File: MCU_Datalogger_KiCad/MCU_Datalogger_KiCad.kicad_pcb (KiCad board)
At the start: 2 copper layers, 29 parts, among them J1 Conn_01x04_Male, J2 Conn_01x04_Male, J3 Conn_01x09_Male, J4 Conn_02x03_Odd_Even, U1 24LC1025, U2 DS1337S+, U3 24LC1025, U4 ATMEGA328P-AU, Y1 32.768 KHz, Y2 16 MHz

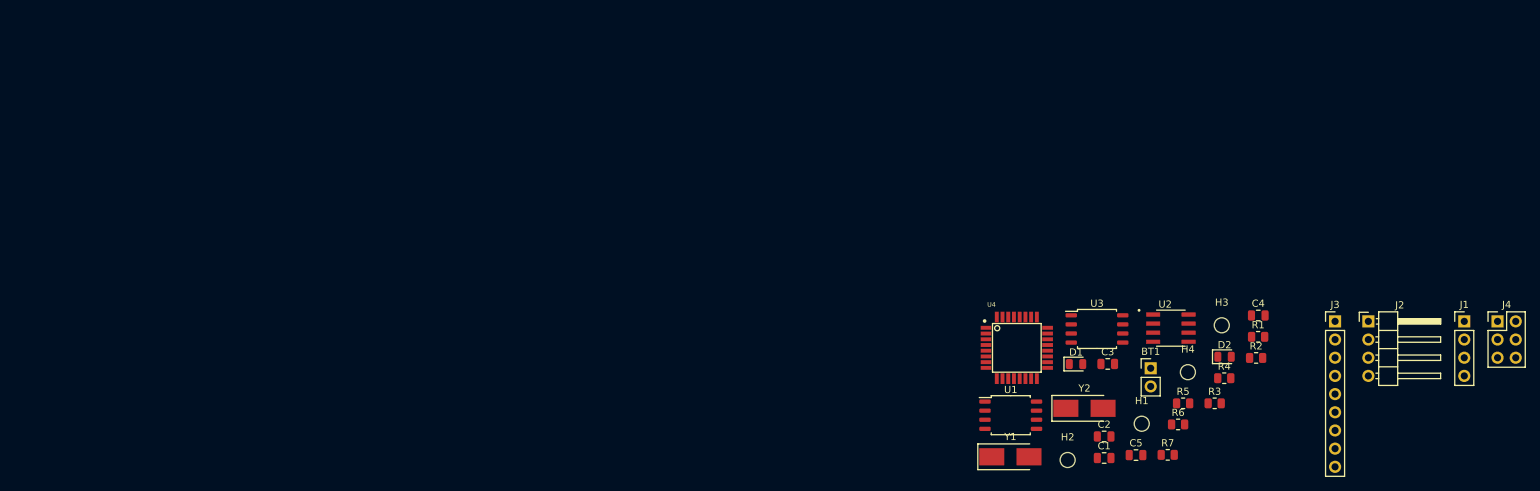
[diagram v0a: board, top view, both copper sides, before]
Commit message: Placement of footprints
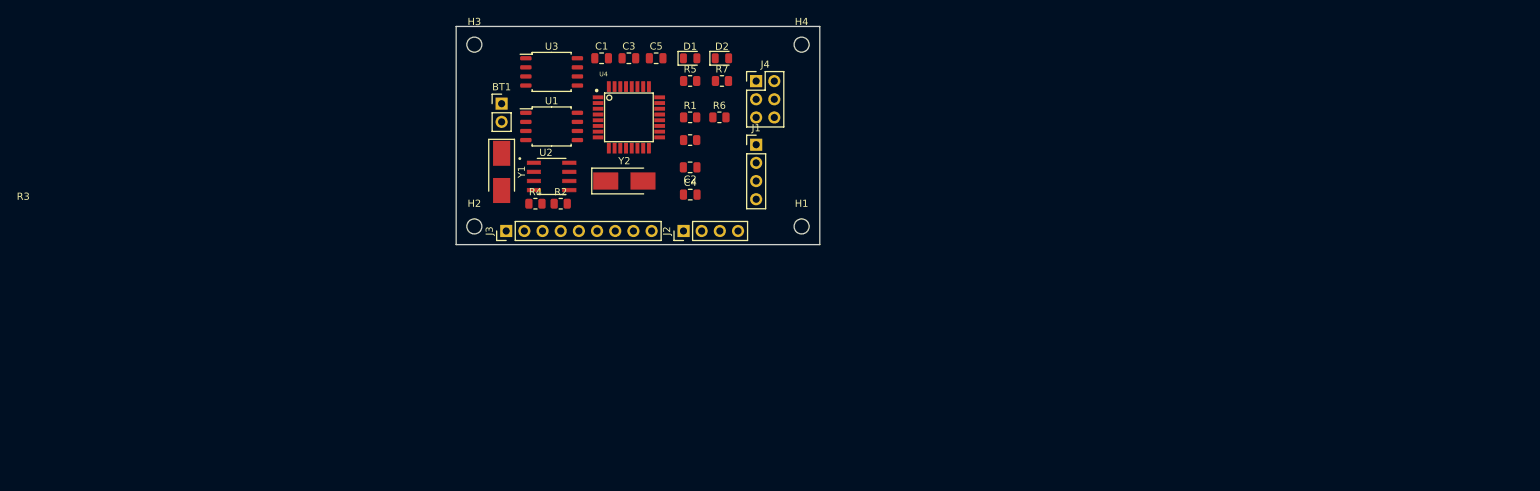
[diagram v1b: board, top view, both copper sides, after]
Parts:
- J2: footprint Connector_PinHeader_2.54mm:PinHeader_1x04_P2.54mm_Horizontal -> Connector_PinHeader_2.54mm:PinHeader_1x04_P2.54mm_Vertical
- moved J3 116.5 mm to (32.4, 66.7), turned to 90 degrees
- moved H3 111.5 mm to (27.9, 40.6)
- moved J4 108.9 mm to (67.3, 45.7)
- moved J1 102.0 mm to (67.3, 54.6)
- moved R2 99.5 mm to (40.0, 62.9)
- moved R4 99.3 mm to (36.5, 62.9)
- moved BT1 97.9 mm to (31.8, 48.9)
- moved J2 96.5 mm to (57.2, 66.7), turned to 90 degrees
- moved C1 89.7 mm to (45.7, 42.5)
- moved H2 89.1 mm to (27.9, 66.0)
- moved U2 89.1 mm to (38.7, 59.1)
- moved C5 87.0 mm to (53.3, 42.5)
- moved R1 85.1 mm to (58.1, 50.8)
- moved U3 84.2 mm to (38.7, 44.5)
- moved R5 82.3 mm to (58.1, 45.7)
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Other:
- board outline added: 50.8 x 30.5 mm

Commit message: Routing
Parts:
- moved D1 4.41 mm to (62.5, 42.9)
- moved R4 4.17 mm to (40.6, 63.0)
- moved D2 4.11 mm to (58.4, 42.7)
- moved H1 3.78 mm to (70.9, 68.6)
- moved H2 2.96 mm to (29.5, 68.6)
- moved R3 2.93 mm to (57.9, 51.1), turned to 180 degrees
- moved R2 2.92 mm to (37.1, 63.0), turned to 180 degrees
- moved H4 2.90 mm to (70.9, 41.4)
- moved R1 2.80 mm to (57.9, 53.6), turned to 180 degrees
- moved J3 2.17 mm to (34.6, 66.8)
- moved H3 1.70 mm to (29.5, 41.4)
- moved J1 1.60 mm to (68.8, 55.1)
- moved J2 1.53 mm to (58.7, 66.8)
- moved C4 1.40 mm to (58.2, 60.2), turned to 180 degrees
- moved J4 1.14 mm to (66.3, 46.2)
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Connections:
- D1 pad 2: /SDK -> /SCK
- U4 pad 17: /SDK -> /SCK
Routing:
- net /Vcc: track 0.00 -> 84.1 mm
- net /SCK: track 0.00 -> 80.0 mm, vias 0 -> 5
- net GND: track 0.00 -> 63.7 mm, vias 0 -> 4
- net Net-(BT1-Pad1): track 0.00 -> 57.2 mm, vias 0 -> 2
- net /SDA: track 0.00 -> 55.9 mm, vias 0 -> 4
- net /TX: track 0.00 -> 35.2 mm, vias 0 -> 1
- net /RX: track 0.00 -> 32.1 mm, vias 0 -> 1
- net /D3: track 0.00 -> 28.5 mm, vias 0 -> 1
- net /D2: track 0.00 -> 27.4 mm, vias 0 -> 1
- net Net-(C3-Pad2): track 0.00 -> 27.1 mm, vias 0 -> 2
- net /MOSI: track 0.00 -> 26.4 mm
- net /RESET: track 0.00 -> 23.5 mm, vias 0 -> 2
- net Net-(C2-Pad2): track 0.00 -> 22.6 mm
- net /D4: track 0.00 -> 22.1 mm, vias 0 -> 1
- net /MISO: track 0.00 -> 19.9 mm, vias 0 -> 2
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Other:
- board size 50.8 x 30.5 mm -> 47 x 32.8 mm

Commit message: Finished routing
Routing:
- net GND: track 63.7 -> 111.0 mm, vias 4 -> 8
- net /Vcc: track 84.1 -> 100.3 mm, vias 0 -> 2
- net /SCK: track 80.0 -> 83.6 mm, vias 5 -> 7
- net Net-(BT1-Pad1): track 57.2 -> 54.3 mm
- net /D4: track 22.1 -> 24.7 mm
- net Net-(C3-Pad2): track 27.1 -> 29.2 mm
- net /D3: track 28.5 -> 27.1 mm
- net /D2: track 27.4 -> 26.7 mm
- net /RESET: track 23.5 -> 23.0 mm
- net /SDA: track 55.9 -> 55.6 mm, vias 4 -> 5
- added copper zone on F.Cu, net /Vcc
- added copper zone on B.Cu, net GND
